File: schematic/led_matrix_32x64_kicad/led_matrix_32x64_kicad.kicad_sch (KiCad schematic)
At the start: 6 parts, among them J1 LED Interface, J2 RTC, J3 INTERFACE, SW3 RESET, U1 Pico

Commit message: Snapshot before flipping the board
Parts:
- added C2, C3: 1u, Capacitor_SMD:C_0805_2012Metric_Pad1.18x1.45mm_HandSolder, symbol Device:C
- added J4: LEDPWR, Connector_PinHeader_2.54mm:PinHeader_1x02_P2.54mm_Horizontal, symbol Connector:Conn_01x02_Male
- added R1: 10k, Resistor_SMD:R_0805_2012Metric_Pad1.20x1.40mm_HandSolder, symbol Device:R
- added U2: NCP380, Package_SO:TSOP-5_1.65x3.05mm_P0.95mm, symbol Matt:NCP380
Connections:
- net 5V: now also C3.1, R1.2, U2.5 (IN); no longer C1.1
- net GND: now also C2.2, C3.2, J4.2 (Pin_2), U2.2 (GND)
- net OVR: now reaches U1.29 (GPIO22)
- net OVR: now also U2.3 (~{FLAG})
- new net EN: R1.1, U2.4 (EN)
- new net OUT: C1.1, C2.1, J4.1 (Pin_1), U2.1 (OUT)
- no-connect marks 15 -> 14
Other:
- moved on the sheet: C1

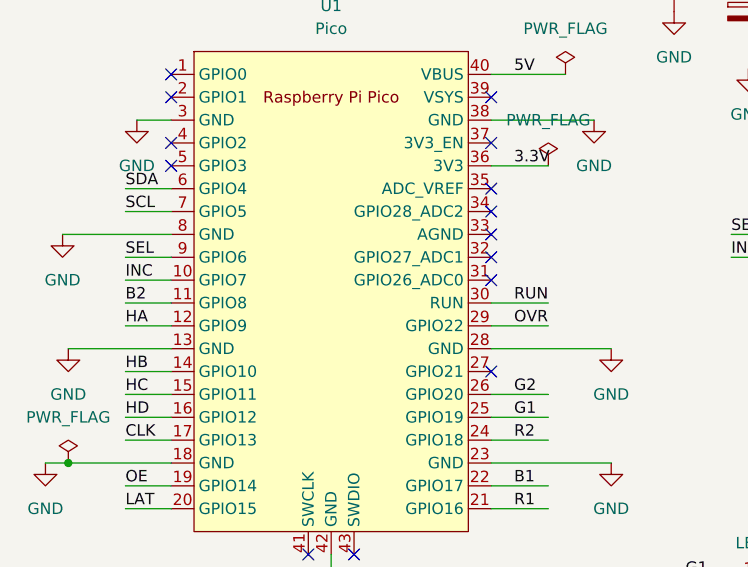
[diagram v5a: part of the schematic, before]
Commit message: New layout is getting closer
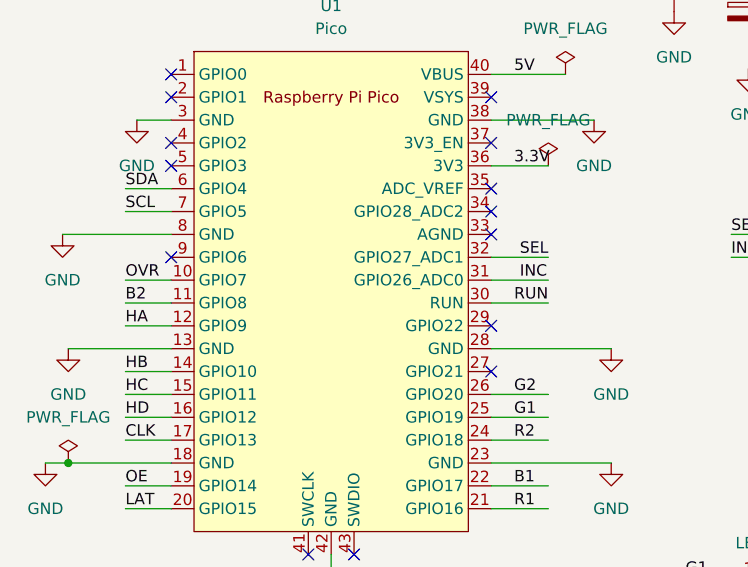
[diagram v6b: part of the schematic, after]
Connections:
- net INC: now also U1.31 (GPIO26_ADC0); no longer U1.10 (GPIO7)
- net OVR: now also U1.10 (GPIO7); no longer U1.29 (GPIO22)
- net SEL: now also U1.32 (GPIO27_ADC1); no longer U1.9 (GPIO6)
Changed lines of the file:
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@@
   )
   (no_connect (at 128.27 95.25))
-  (no_connect (at 128.27 100.33))
+  (no_connect (at 128.27 105.41))
   (no_connect (at 92.71 80.01))
   (no_connect (at 107.95 130.81))
   (no_connect (at 92.71 87.63))
   (no_connect (at 92.71 77.47))
+  (no_connect (at 92.71 97.79))
   (no_connect (at 128.27 92.71))
-  (no_connect (at 128.27 97.79))
   (no_connect (at 128.27 110.49))
   (no_connect (at 128.27 85.09))
@@
     (stroke (width 0) (type default) (color 0 0 0 0))
   )
+  (wire (pts (xy 128.27 82.55) (xy 139.7 82.55))
+    (stroke (width 0) (type default) (color 0 0 0 0))
+  )
+  (wire (pts (xy 196.215 62.865) (xy 203.2 62.865))
+    (stroke (width 0) (type default) (color 0 0 0 0))
+  )
+  (wire (pts (xy 160.655 65.405) (xy 160.655 58.42))
+    (stroke (width 0) (type default) (color 0 0 0 0))
+  )
+  (wire (pts (xy 167.64 135.89) (xy 173.99 135.89))
+    (stroke (width 0) (type default) (color 0 0 0 0))
+  )
+  (wire (pts (xy 167.64 143.51) (xy 173.99 143.51))
+    (stroke (width 0) (type default) (color 0 0 0 0))
+  )
+  (wire (pts (xy 149.86 135.89) (xy 154.94 135.89))
+    (stroke (width 0) (type default) (color 0 0 0 0))
+  )
+  (wire (pts (xy 149.86 146.05) (xy 154.94 146.05))
+    (stroke (width 0) (type default) (color 0 0 0 0))
+  )
+  (wire (pts (xy 182.245 112.395) (xy 187.325 112.395))
+    (stroke (width 0) (type default) (color 0 0 0 0))
+  )
+  (wire (pts (xy 128.27 125.73) (xy 134.62 125.73))
+    (stroke (width 0) (type default) (color 0 0 0 0))
+  )
+  (wire (pts (xy 156.845 62.865) (xy 156.845 66.675))
+    (stroke (width 0) (type default) (color 0 0 0 0))
+  )
+  (wire (pts (xy 87.63 110.49) (xy 92.71 110.49))
+    (stroke (width 0) (type default) (color 0 0 0 0))
+  )
+  (wire (pts (xy 149.86 133.35) (xy 154.94 133.35))
+    (stroke (width 0) (type default) (color 0 0 0 0))
+  )
+  (wire (pts (xy 186.69 88.265) (xy 186.69 90.805))
+    (stroke (width 0) (type default) (color 0 0 0 0))
+  )
+  (wire (pts (xy 87.63 102.87) (xy 92.71 102.87))
+    (stroke (width 0) (type default) (color 0 0 0 0))
+  )
+  (wire (pts (xy 149.86 143.51) (xy 154.94 143.51))
+    (stroke (width 0) (type default) (color 0 0 0 0))
+  )
+  (wire (pts (xy 188.595 62.865) (xy 196.215 62.865))
+    (stroke (width 0) (type default) (color 0 0 0 0))
+  )
+  (wire (pts (xy 128.27 100.33) (xy 134.62 100.33))
+    (stroke (width 0) (type default) (color 0 0 0 0))
+  )
+  (wire (pts (xy 87.63 123.19) (xy 92.71 123.19))
+    (stroke (width 0) (type default) (color 0 0 0 0))
+  )
+  (wire (pts (xy 87.63 118.11) (xy 92.71 118.11))
+    (stroke (width 0) (type default) (color 0 0 0 0))
+  )
+  (wire (pts (xy 167.64 140.97) (xy 173.99 140.97))
+    (stroke (width 0) (type default) (color 0 0 0 0))
+  )
   (wire (pts (xy 87.63 100.33) (xy 92.71 100.33))
     (stroke (width 0) (type default) (color 0 0 0 0))
   )
-  (wire (pts (xy 128.27 82.55) (xy 139.7 82.55))
-    (stroke (width 0) (type default) (color 0 0 0 0))
-  )
-  (wire (pts (xy 196.215 62.865) (xy 203.2 62.865))
-    (stroke (width 0) (type default) (color 0 0 0 0))
-  )
-  (wire (pts (xy 160.655 65.405) (xy 160.655 58.42))
-    (stroke (width 0) (type default) (color 0 0 0 0))
-  )
-  (wire (pts (xy 167.64 135.89) (xy 173.99 135.89))
-    (stroke (width 0) (type default) (color 0 0 0 0))
-  )
-  (wire (pts (xy 167.64 143.51) (xy 173.99 143.51))
-    (stroke (width 0) (type default) (color 0 0 0 0))
-  )
-  (wire (pts (xy 149.86 135.89) (xy 154.94 135.89))
-    (stroke (width 0) (type default) (color 0 0 0 0))
-  )
-  (wire (pts (xy 149.86 146.05) (xy 154.94 146.05))
-    (stroke (width 0) (type default) (color 0 0 0 0))
-  )
-  (wire (pts (xy 182.245 112.395) (xy 187.325 112.395))
-    (stroke (width 0) (type default) (color 0 0 0 0))
-  )
-  (wire (pts (xy 128.27 125.73) (xy 134.62 125.73))
-    (stroke (width 0) (type default) (color 0 0 0 0))
-  )
-  (wire (pts (xy 156.845 62.865) (xy 156.845 66.675))
-    (stroke (width 0) (type default) (color 0 0 0 0))
-  )
-  (wire (pts (xy 87.63 110.49) (xy 92.71 110.49))
-    (stroke (width 0) (type default) (color 0 0 0 0))
-  )
-  (wire (pts (xy 149.86 133.35) (xy 154.94 133.35))
-    (stroke (width 0) (type default) (color 0 0 0 0))
-  )
-  (wire (pts (xy 186.69 88.265) (xy 186.69 90.805))
-    (stroke (width 0) (type default) (color 0 0 0 0))
-  )
-  (wire (pts (xy 87.63 102.87) (xy 92.71 102.87))
-    (stroke (width 0) (type default) (color 0 0 0 0))
-  )
-  (wire (pts (xy 149.86 143.51) (xy 154.94 143.51))
-    (stroke (width 0) (type default) (color 0 0 0 0))
-  )
-  (wire (pts (xy 188.595 62.865) (xy 196.215 62.865))
-    (stroke (width 0) (type default) (color 0 0 0 0))
-  )
-  (wire (pts (xy 87.63 97.79) (xy 92.71 97.79))
-    (stroke (width 0) (type default) (color 0 0 0 0))
-  )
-  (wire (pts (xy 87.63 123.19) (xy 92.71 123.19))
-    (stroke (width 0) (type default) (color 0 0 0 0))
-  )
-  (wire (pts (xy 87.63 118.11) (xy 92.71 118.11))
-    (stroke (width 0) (type default) (color 0 0 0 0))
-  )
-  (wire (pts (xy 167.64 140.97) (xy 173.99 140.97))
-    (stroke (width 0) (type default) (color 0 0 0 0))
-  )
-  (wire (pts (xy 128.27 105.41) (xy 134.62 105.41))
-    (stroke (width 0) (type default) (color 0 0 0 0))
-  )
   (wire (pts (xy 163.195 65.405) (xy 163.195 70.485))
     (stroke (width 0) (type default) (color 0 0 0 0))
@@
     (stroke (width 0) (type default) (color 0 0 0 0))
   )
+  (wire (pts (xy 128.27 97.79) (xy 134.62 97.79))
+    (stroke (width 0) (type default) (color 0 0 0 0))
+  )
   (wire (pts (xy 149.86 148.59) (xy 154.94 148.59))
     (stroke (width 0) (type default) (color 0 0 0 0))
@@
     (effects (font (size 1.27 1.27)) (justify left bottom))
   )
-  (label "OVR" (at 130.81 105.41 0)
+  (label "OVR" (at 87.63 100.33 0)
     (effects (font (size 1.27 1.27)) (justify left bottom))
   )
@@
     (effects (font (size 1.27 1.27)) (justify left bottom))
   )
-  (label "SEL" (at 87.63 97.79 0)
+  (label "SEL" (at 131.445 97.79 0)
     (effects (font (size 1.27 1.27)) (justify left bottom))
   )
@@
     (effects (font (size 1.27 1.27)) (justify left bottom))
   )
-  (label "INC" (at 87.63 100.33 0)
-    (effects (font (size 1.27 1.27)) (justify left bottom))
-  )
+  (label "INC" (at 131.445 100.33 0)
+    (effects (font (size 1.27 1.27)) (justify left bottom))
+  )

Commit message: More progress on PCB
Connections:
- net GND: now also J4.1 (Pin_1); no longer J4.2 (Pin_2), U2.2 (GND)
- net OUT: now also J4.2 (Pin_2); no longer J4.1 (Pin_1)
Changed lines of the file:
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@@
     (company "Matt Wachowski")
   )
-  (junction (at 163.195 65.405) (diameter 0) (color 0 0 0 0)
-  )
-  (junction (at 163.195 62.865) (diameter 0) (color 0 0 0 0)
-  )
   (junction (at 196.215 62.865) (diameter 0) (color 0 0 0 0)
   )
+  (junction (at 170.815 62.865) (diameter 0) (color 0 0 0 0)
+  )
+  (junction (at 81.28 120.65) (diameter 0) (color 0 0 0 0)
+  )
   (junction (at 156.845 62.865) (diameter 0) (color 0 0 0 0)
   )
-  (junction (at 81.28 120.65) (diameter 0) (color 0 0 0 0)
-  )
-  (junction (at 170.815 62.865) (diameter 0) (color 0 0 0 0)
+  (junction (at 160.655 62.865) (diameter 0) (color 0 0 0 0)
   )
   (no_connect (at 128.27 95.25))
@@
     (stroke (width 0) (type default) (color 0 0 0 0))
   )
-  (wire (pts (xy 163.195 62.865) (xy 156.845 62.865))
-    (stroke (width 0) (type default) (color 0 0 0 0))
-  )
   (wire (pts (xy 182.245 117.475) (xy 187.325 117.475))
     (stroke (width 0) (type default) (color 0 0 0 0))
@@
     (stroke (width 0) (type default) (color 0 0 0 0))
   )
-  (wire (pts (xy 163.195 62.865) (xy 163.195 58.42))
-    (stroke (width 0) (type default) (color 0 0 0 0))
-  )
   (wire (pts (xy 165.735 67.945) (xy 170.815 67.945))
     (stroke (width 0) (type default) (color 0 0 0 0))
@@
     (stroke (width 0) (type default) (color 0 0 0 0))
   )
+  (wire (pts (xy 156.845 62.865) (xy 160.655 62.865))
+    (stroke (width 0) (type default) (color 0 0 0 0))
+  )
   (wire (pts (xy 196.215 62.865) (xy 203.2 62.865))
     (stroke (width 0) (type default) (color 0 0 0 0))
   )
-  (wire (pts (xy 160.655 65.405) (xy 160.655 58.42))
-    (stroke (width 0) (type default) (color 0 0 0 0))
-  )
   (wire (pts (xy 167.64 135.89) (xy 173.99 135.89))
     (stroke (width 0) (type default) (color 0 0 0 0))
@@
     (stroke (width 0) (type default) (color 0 0 0 0))
   )
+  (wire (pts (xy 170.815 62.865) (xy 171.45 62.865))
+    (stroke (width 0) (type default) (color 0 0 0 0))
+  )
   (wire (pts (xy 87.63 110.49) (xy 92.71 110.49))
     (stroke (width 0) (type default) (color 0 0 0 0))
@@
     (stroke (width 0) (type default) (color 0 0 0 0))
   )
-  (wire (pts (xy 163.195 65.405) (xy 163.195 70.485))
+  (wire (pts (xy 163.195 58.42) (xy 163.195 70.485))
     (stroke (width 0) (type default) (color 0 0 0 0))
   )
@@
     (stroke (width 0) (type default) (color 0 0 0 0))
   )
-  (wire (pts (xy 163.195 65.405) (xy 160.655 65.405))
-    (stroke (width 0) (type default) (color 0 0 0 0))
-  )
   (wire (pts (xy 156.845 74.295) (xy 156.845 76.835))
     (stroke (width 0) (type default) (color 0 0 0 0))
   )
-  (wire (pts (xy 170.815 65.405) (xy 163.195 65.405))
-    (stroke (width 0) (type default) (color 0 0 0 0))
-  )
   (wire (pts (xy 87.63 115.57) (xy 92.71 115.57))
     (stroke (width 0) (type default) (color 0 0 0 0))
   )
-  (wire (pts (xy 171.45 62.865) (xy 170.815 62.865))
+  (wire (pts (xy 160.655 62.865) (xy 170.815 62.865))
     (stroke (width 0) (type default) (color 0 0 0 0))
   )
@@
     (stroke (width 0) (type default) (color 0 0 0 0))
   )
+  (wire (pts (xy 160.655 62.865) (xy 160.655 58.42))
+    (stroke (width 0) (type default) (color 0 0 0 0))
+  )
   (wire (pts (xy 167.64 138.43) (xy 173.99 138.43))
     (stroke (width 0) (type default) (color 0 0 0 0))
@@
     (stroke (width 0) (type default) (color 0 0 0 0))
   )
-  (wire (pts (xy 170.815 62.865) (xy 163.195 62.865))
-    (stroke (width 0) (type default) (color 0 0 0 0))
-  )

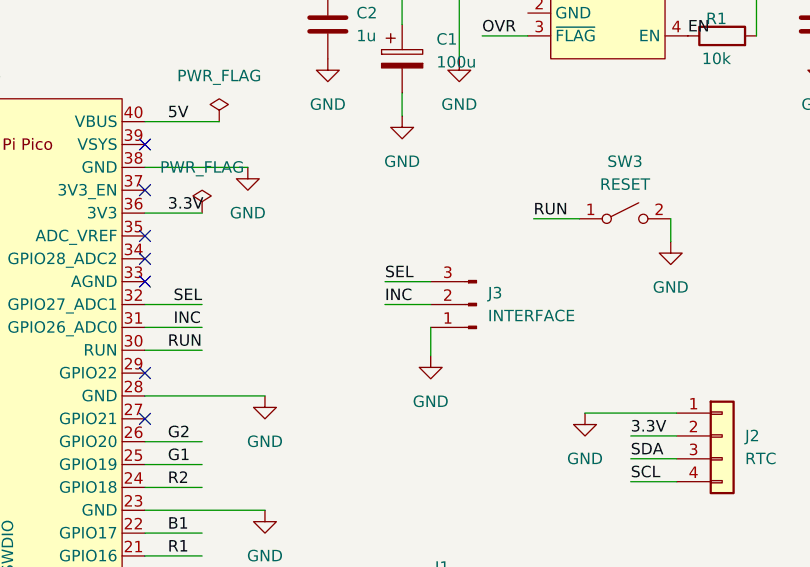
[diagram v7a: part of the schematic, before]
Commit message: Moved RTC clock pins.  Worked on labeling.
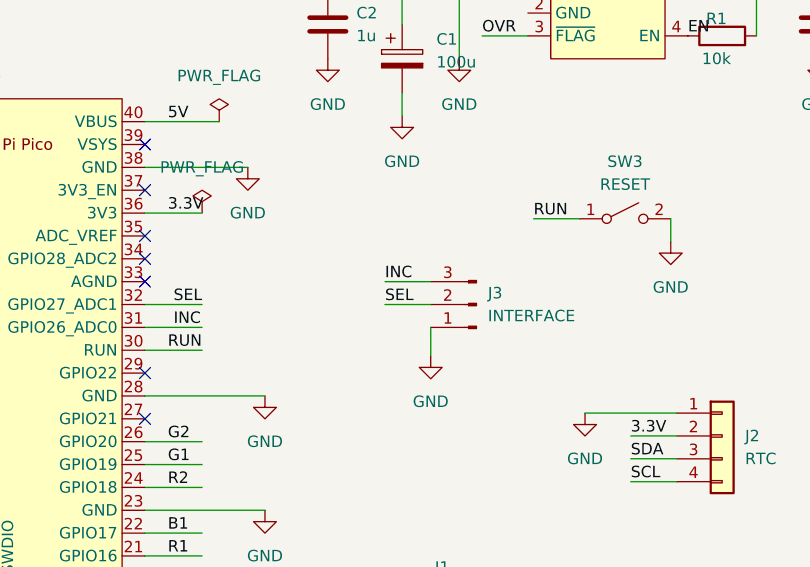
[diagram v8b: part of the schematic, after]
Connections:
- net INC: now also J3.3 (Pin_3); no longer J3.2 (Pin_2)
- net SEL: now also J3.2 (Pin_2); no longer J3.3 (Pin_3)
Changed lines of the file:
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@@
     (effects (font (size 1.27 1.27)) (justify left bottom))
   )
-  (label "SEL" (at 154.94 95.25 0)
+  (label "INC" (at 154.94 95.25 0)
     (effects (font (size 1.27 1.27)) (justify left bottom))
   )
@@
     (effects (font (size 1.27 1.27)) (justify left bottom))
   )
-  (label "INC" (at 154.94 97.79 0)
+  (label "SEL" (at 154.94 97.79 0)
     (effects (font (size 1.27 1.27)) (justify left bottom))
   )
